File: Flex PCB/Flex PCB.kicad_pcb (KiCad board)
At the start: 2 copper layers, 52.2 x 54 mm, 5 parts, among them J1 FPC_Male, J2 Test_Headers

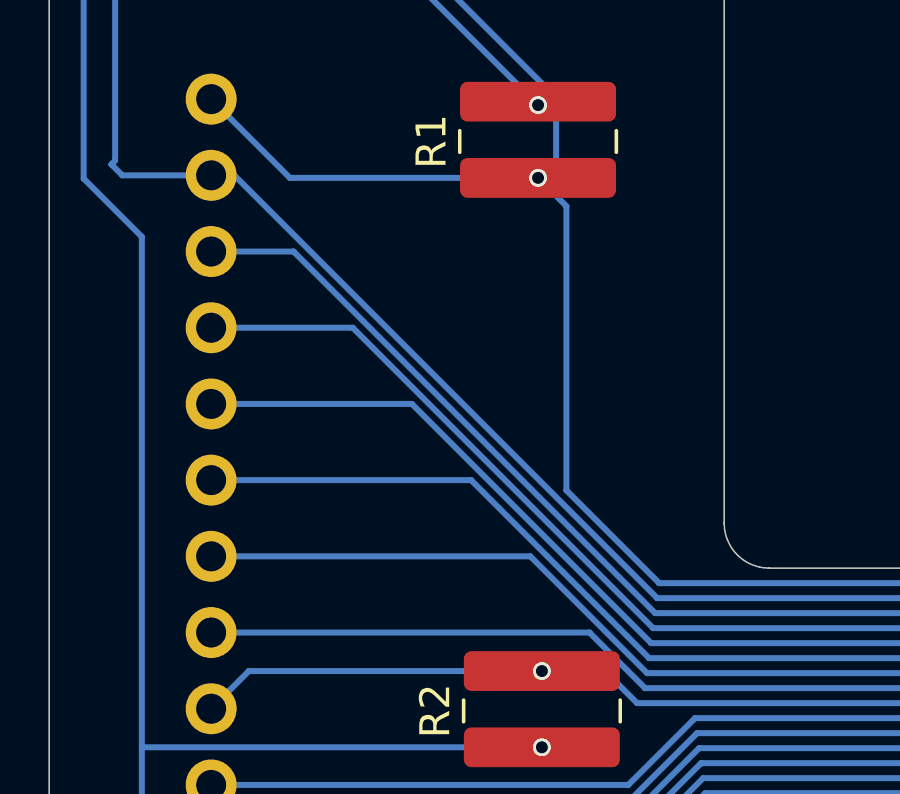
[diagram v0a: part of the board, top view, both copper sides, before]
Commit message: updated silkscreen thickness + gerbers
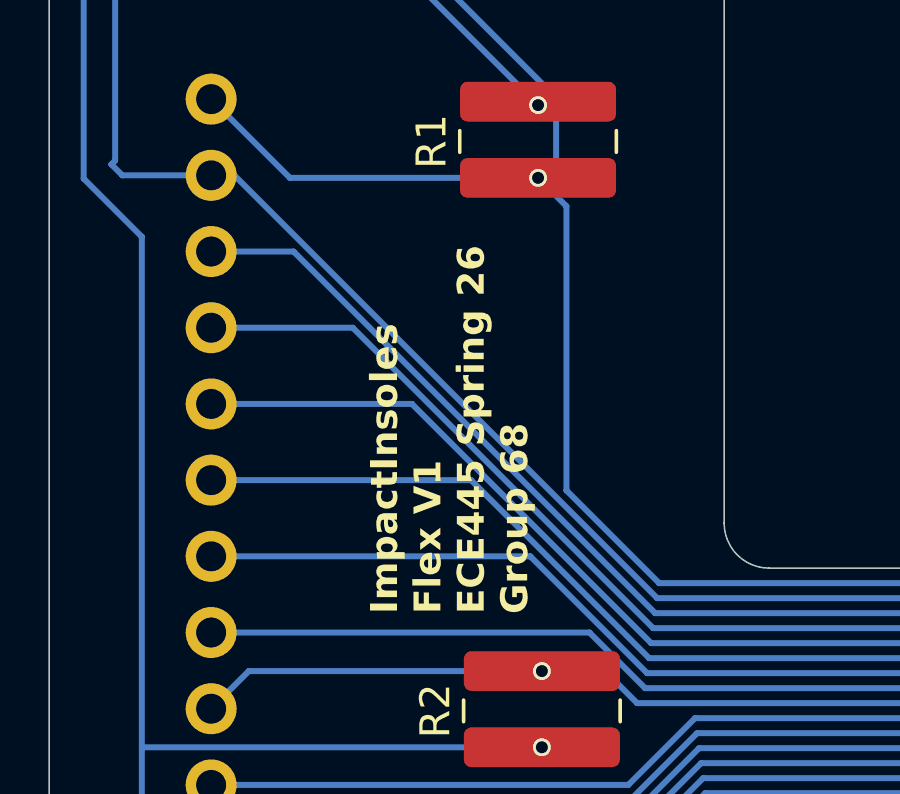
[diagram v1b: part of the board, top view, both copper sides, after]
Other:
- board text added: "ImpactInsoles Flex V1 ECE445 Spring 26 Group 68"
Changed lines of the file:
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@@
 		(layer "Edge.Cuts")
+	)
+	(gr_text "ImpactInsoles\nFlex V1\nECE445 Spring 26\nGroup 68\n"
+		(at 153.543 81.026 90)
+		(layer "F.SilkS")
+		(effects
+			(font
+				(size 0.8984 0.8984)
+				(thickness 0.14986)
+				(bold yes)
+			)
+			(justify left bottom)
+		)
 	)
 	(gr_text "Stiffener TOP"
@@
 			(keep_text_aligned yes)
 		)
-		(gr_text "3.5"
+		(gr_text "137.7953"
 			(at 191.5 94.35 0)
 			(layer "Cmts.User")

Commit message: Flex PCB v2
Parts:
- added R4: FSR1, Resistor_SMD:FSR_402, F.Cu at (153.5, 113.0)
- added R5: FSR1, Resistor_SMD:FSR_402, F.Cu at (153.5, 55.3)
- added R6: FSR1, Resistor_SMD:FSR_402, F.Cu at (153.5, 46.8)
- added R7: FSR1, Resistor_SMD:FSR_402, F.Cu at (153.5, 121.5)
- J1: footprint Connector_FFC-FPC:FPC-Male-18P-0.5mm -> Connector_FFC-FPC:FPC-Male-18P-1mm
- moved J1 22.8 mm to (214.5, 84.4)
- moved R1 0.76 mm to (153.6, 66.0)
- moved R3 0.52 mm to (153.8, 103.3)
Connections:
- J1 pad 1: Net-(J1-Pin_1) -> /3V3
- J1 pad 18: /3V3 -> /GND
- J2 pad 1: Net-(J1-Pin_1) -> /3V3
- J2 pad 18: /3V3 -> /GND
- R1 pad 2: Net-(J1-Pin_17) -> Net-(J1-Pin_15)
- R3 pad 2: Net-(J1-Pin_2) -> Net-(J1-Pin_4)
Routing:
- net /GND: track 0.00 -> 121.3 mm
- net /3V3: track 155.9 -> 240.7 mm
- net Net-(J1-Pin_1): track 67.1 -> 0.00 mm
- net Net-(J1-Pin_16): track 54.1 -> 104.4 mm, vias 0 -> 1
- net Net-(J1-Pin_2): track 63.8 -> 110.5 mm
- net Net-(J1-Pin_17): track 79.7 -> 121.6 mm
- net Net-(J1-Pin_15): track 53.2 -> 85.8 mm, vias 0 -> 1
- net Net-(J1-Pin_3): track 62.6 -> 93.7 mm, vias 0 -> 1
- net Net-(J1-Pin_9): track 50.0 -> 73.2 mm
- net Net-(J1-Pin_4): track 60.6 -> 82.9 mm, vias 0 -> 1
- net Net-(J1-Pin_10): track 50.1 -> 72.4 mm
- net Net-(J1-Pin_11): track 49.9 -> 72.0 mm
- net Net-(J1-Pin_12): track 50.7 -> 72.6 mm
- net Net-(J1-Pin_13): track 51.6 -> 73.2 mm
- net Net-(J1-Pin_14): track 52.4 -> 73.9 mm
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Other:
- board size 52.2 x 54 mm -> 74.8 x 83 mm
- board text added: "ImpactInsoles Flex V2 ECE445 Spring 26 Group 68"
- board text removed: "ImpactInsoles Flex V1 ECE445 Spring 26 Group 68"

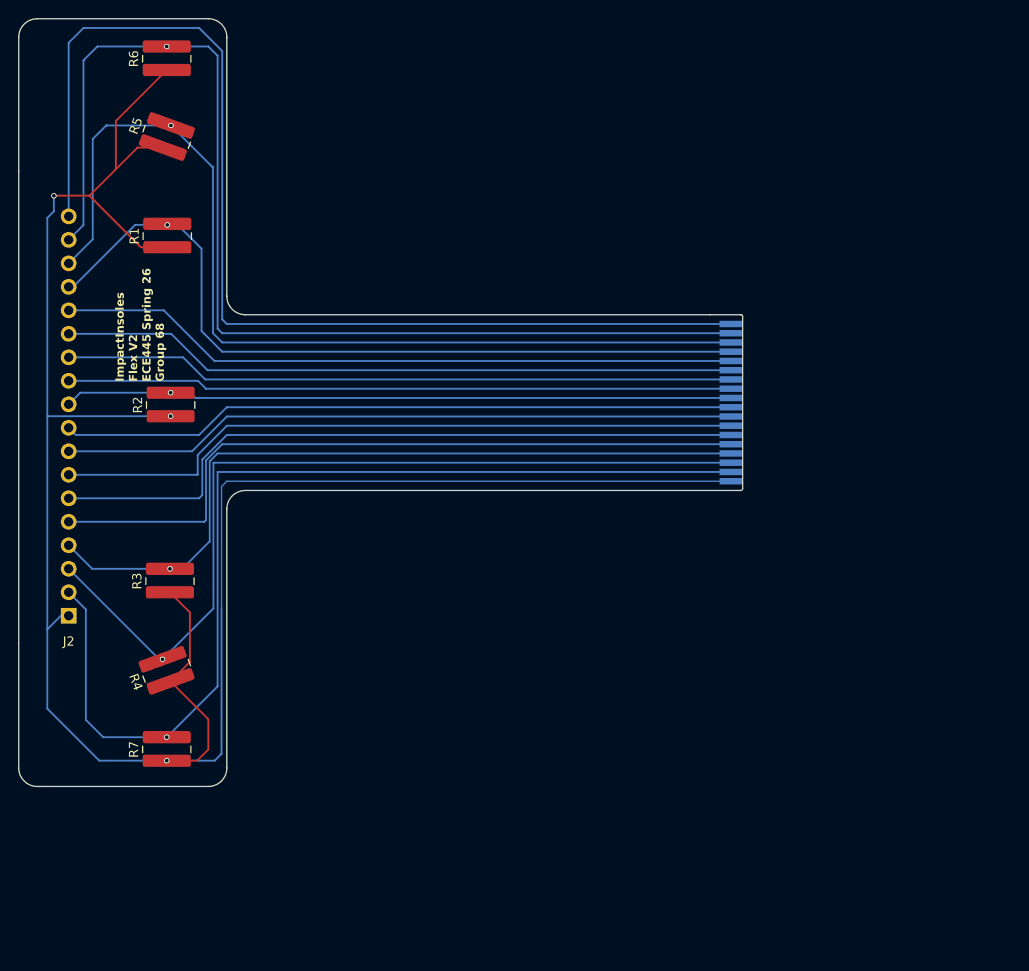
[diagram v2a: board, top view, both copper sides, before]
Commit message: Flex Hub PCB
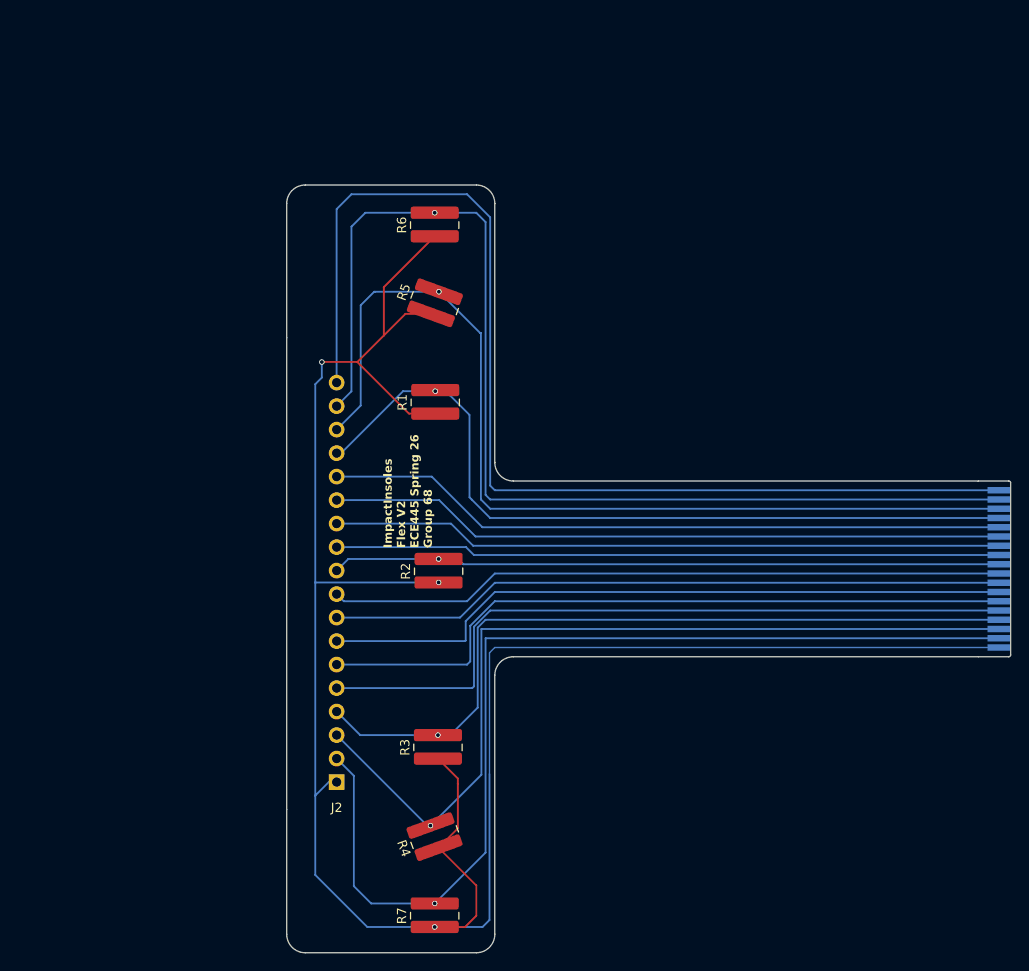
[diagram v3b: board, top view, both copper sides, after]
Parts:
- moved J1 34.1 mm to (243.4, 102.4)
- moved J2 34.1 mm to (171.9, 125.0)
- moved R1 34.1 mm to (182.5, 84.0)
- moved R2 34.1 mm to (182.9, 102.2)
- moved R3 34.1 mm to (182.8, 121.3)
- moved R4 34.1 mm to (182.5, 131.0)
- moved R5 34.1 mm to (182.5, 73.3)
- moved R6 34.1 mm to (182.5, 64.8)
- moved R7 34.1 mm to (182.5, 139.5)
